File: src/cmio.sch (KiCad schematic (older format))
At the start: 3 parts

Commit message: Add LDO for 2.8V and 1.8V
Signed-off-by: Mahyar Koshkouei <deltabeard@users.noreply.github.com>
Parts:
- removed J?: TVOUT, symbol CONN_01X01_MALE
- added C1, C2, C5, C6: 1uF, symbol C_Small
- added C3, C4: 10nF, symbol C_Small
- added J2: USB_OTG, symbol USB_OTG
- added J4: CONN_COAXIAL, Connect:BNC, symbol CONN_COAXIAL
- added J5: CONN_02X20, Socket_Strips:Socket_Strip_Straight_2x20_Pitch2.54mm, symbol CONN_02X20
- added J6: Micro_SD_Card_TFP09_2_12B, symbol Micro_SD_Card_TFP09_2_12B
- added JP1: TP, Pin_Headers:Pin_Header_Straight_1x02_Pitch2.54mm, symbol Jumper_NC_Small
- added JP2: Disable SD Card, Pin_Headers:Pin_Header_Straight_1x02_Pitch2.54mm, symbol Jumper_NO_Small
- added SW1: SW_Push, Buttons_Switches_SMD:SW_SPST_TL3342, symbol SW_Push
- added U1: LD3985M18R, TO_SOT_Packages_SMD:SOT-23-5, symbol LD3985M18R
- added U2: LD3985M28R, TO_SOT_Packages_SMD:SOT-23-5, symbol LD3985M28R
- J1: renamed from J?; footprint (none) -> Socket_Strips:Socket_Strip_Straight_2x20_Pitch2.54mm
- gave numbers to parts that had none: 1
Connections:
- net labels added: CLK, CMD, DAT0, DAT1, DAT2, DAT3, DSI0, DSI0_0, DSI0_1, DSI0_2, DSI0_3, DSI0_4, DSI0_5, DSI1_0, DSI1_1, DSI1_2, DSI1_3, DSI1_4, DSI1_5, DSI1_6, DSI1_7, DSI1_8, DSI1_9, G28, G29, G30, G31, G32, G33, G34, G35, G36, G37, G38, G39, G40, G41, G42, G43, G44, G45, OTDIG, TVDAC
- net labels removed: +3.3V
- wire segments 3 -> 107
- no-connect marks 10 -> 46
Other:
- moved on the sheet: J1, J3

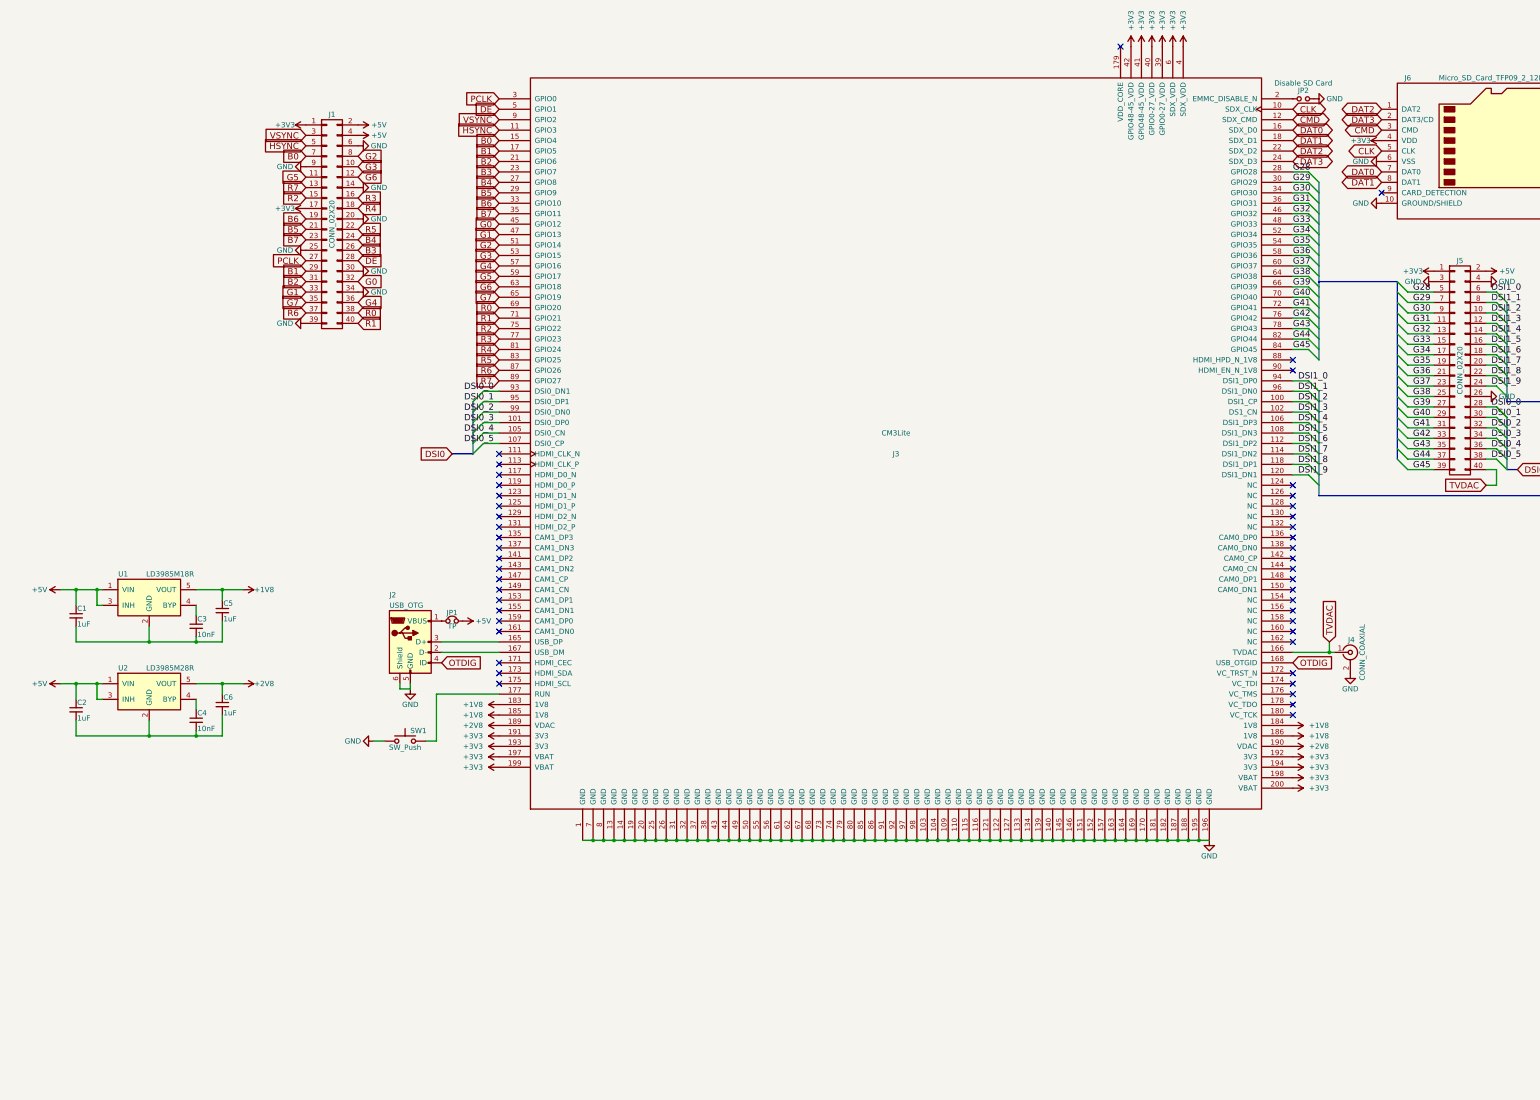
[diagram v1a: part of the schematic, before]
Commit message: Add Micro SD Card Footprint and 20-TQFP
Signed-off-by: Mahyar Koshkouei <deltabeard@users.noreply.github.com>
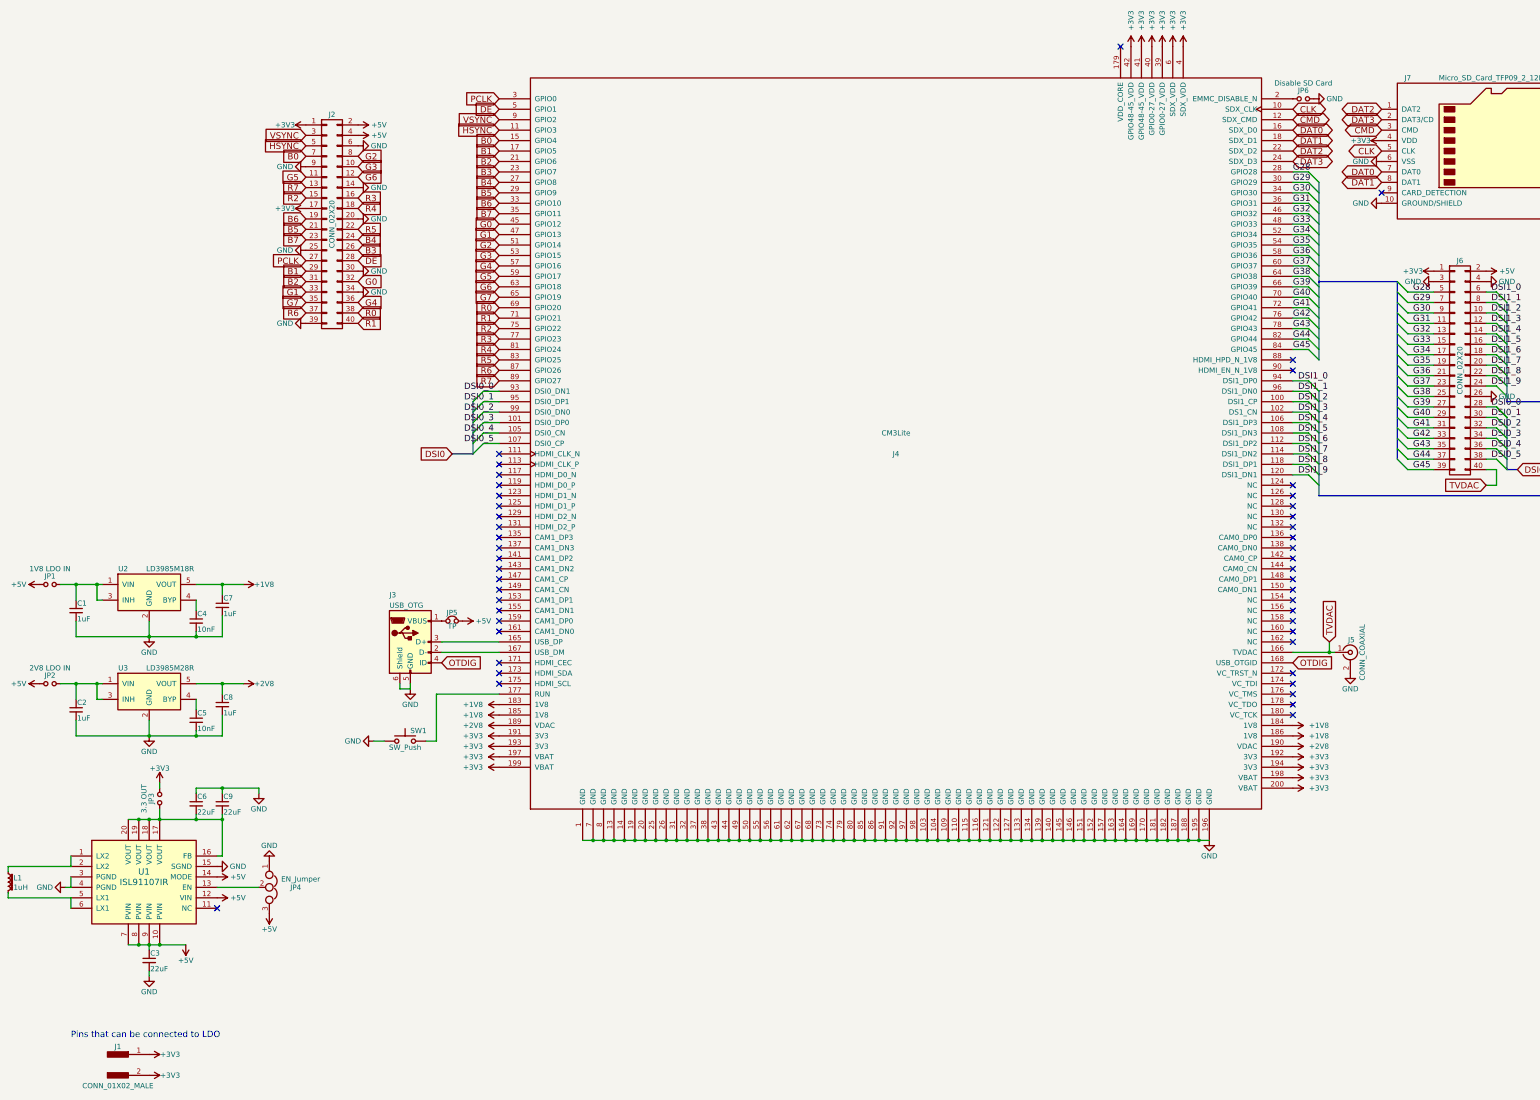
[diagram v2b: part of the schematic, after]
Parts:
- added C3, C6, C9: 22uF, Capacitors_SMD:C_1206_HandSoldering, symbol C_Small
- added J1: CONN_01X02_MALE, Pin_Headers:Pin_Header_Straight_1x02_Pitch2.54mm, symbol CONN_01X02_MALE
- added JP1: 1V8 LDO IN, Pin_Headers:Pin_Header_Straight_1x02_Pitch2.54mm, symbol Jumper_NO_Small
- added JP2: 2V8 LDO IN, Pin_Headers:Pin_Header_Straight_1x02_Pitch2.54mm, symbol Jumper_NO_Small
- added JP3: 3.3 OUT, Pin_Headers:Pin_Header_Straight_1x02_Pitch2.54mm, symbol Jumper_NO_Small
- added JP4: EN_Jumper, Socket_Strips:Socket_Strip_Straight_1x03_Pitch2.54mm, symbol Jumper_NC_Dual
- added L1: 1uH, Inductors:Inductor_Taiyo-Yuden_NR-40xx_HandSoldering, symbol L_Core_Ferrite_Small
- added U1: ISL91107IR, foot:20_TQFP, symbol ISL91107IR
- C1, C2: footprint (none) -> Capacitors_SMD:C_1206_HandSoldering
- C4: renamed from C3; footprint (none) -> Capacitors_SMD:C_1206_HandSoldering
- C5: renamed from C4; footprint (none) -> Capacitors_SMD:C_1206_HandSoldering
- C7: renamed from C5; footprint (none) -> Capacitors_SMD:C_1206_HandSoldering
- C8: renamed from C6; footprint (none) -> Capacitors_SMD:C_1206_HandSoldering
- renumbered J1 to J2, J2 to J3, J3 to J4, J4 to J5, J5 to J6, J6 to J7, JP1 to JP5, JP2 to JP6, U1 to U2, U2 to U3
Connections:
- net +3V3: now also J1.1, J1.2, JP3.2
- net +5V: now also C3.1, JP1.1, JP2.1, JP4.3, U1.10 (PVIN), U1.12 (VIN), U1.14 (MODE), U1.7 (PVIN), U1.8 (PVIN), U1.9 (PVIN); no longer C1.1, C2.1, U2.1 (VIN), U2.3 (INH), U3.1 (VIN), U3.3 (INH)
- net GND: now also C1.2, C2.2, C4.2, C5.2, C7.2, C8.2, U2.2 (GND), U3.2 (GND), C3.2, C6.1, C9.1, JP4.1, U1.15 (SGND), U1.3 (PGND), U1.4 (PGND)
- new net: C1.1, JP1.2, U2.1 (VIN), U2.3 (INH)
- new net: C2.1, JP2.2, U3.1 (VIN), U3.3 (INH)
- new net: L1.1, U1.1 (LX2), U1.2 (LX2)
- new net: JP4.2, U1.13 (EN)
- new net: C6.2, C9.2, JP3.1, U1.16 (FB), U1.17 (VOUT), U1.18 (VOUT), U1.19 (VOUT), U1.20 (VOUT)
- new net: L1.2, U1.5 (LX1), U1.6 (LX1)
- no-connect marks 46 -> 47
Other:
- note added: "Pins that can be connected to LDO"
- moved on the sheet: C1, C4, C7, U2

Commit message: Before removing RPi GPIO Compat
Signed-off-by: Mahyar Koshkouei <deltabeard@users.noreply.github.com>
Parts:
- added J8: CONN_01X06, Pin_Headers:Pin_Header_Straight_1x06_Pitch2.54mm, symbol CONN_01X06
- J3: footprint (none) -> foot:Micro_USB_B_10104110
- J5: footprint Connect:BNC -> foot:RCA_PHONO
- J7: footprint (none) -> foot:TFP09-2-12B
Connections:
- net +1V8: now also J6.34 (P34)
- net +2V8: now also J6.32 (P32)
- net +3V3: now also J6.30 (P30)
- net +5V: now also J6.28 (P28)
- net DSI0_0: now also J8.6 (P6); no longer J6.28 (P28)
- net DSI0_1: now also J8.5 (P5); no longer J6.30 (P30)
- net DSI0_2: now also J8.4 (P4); no longer J6.32 (P32)
- net DSI0_3: now also J8.3 (P3); no longer J6.34 (P34)
- net DSI0_4: now also J8.2 (P2); no longer J6.36 (P36)
- net DSI0_5: now also J8.1 (P1); no longer J6.38 (P38)
- net GND: now also J6.36 (P36), J6.38 (P38)
- net D+: now reaches J3.3 (D+), J4.165 (USB_DP)
- net D-: now reaches J3.2 (D-), J4.167 (USB_DM)
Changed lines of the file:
@@
 LIBS:Zilog
 LIBS:cmio-cache
-EELAYER 25 0
+EELAYER 26 0
 EELAYER END
 $Descr A3 16535 11693
@@
 F 0 "J3" H 4700 7200 50  0000 L CNN
 F 1 "USB_OTG" H 4700 7100 50  0000 L CNN
-F 2 "" H 5050 6700 50  0001 C CNN
+F 2 "foot:Micro_USB_B_10104110" H 5050 6700 50  0001 C CNN
 F 3 "" H 5050 6700 50  0001 C CNN
 	1    4900 6750
@@
 F 0 "J7" H 14450 2750 50  0000 C CNN
 F 1 "Micro_SD_Card_TFP09_2_12B" H 15750 2750 50  0000 R CNN
-F 2 "" H 17150 2750 50  0001 C CNN
+F 2 "foot:TFP09-2-12B" H 17150 2750 50  0001 C CNN
 F 3 "" H 15100 2150 50  0001 C CNN
 	1    15100 2050
@@
 F 0 "J5" H 13910 6970 50  0000 C CNN
 F 1 "CONN_COAXIAL" V 14015 6850 50  0000 C CNN
-F 2 "Connect:BNC" H 13900 6850 50  0001 C CNN
+F 2 "foot:RCA_PHONO" H 13900 6850 50  0001 C CNN
 F 3 "" H 13900 6850 50  0001 C CNN
 	1    13900 6850
@@
 Entry Wire Line
 	5500 4950 5600 4850
-Text GLabel 5300 4950 0    60   Input ~ 0
-DSI0
 Text Label 5700 4350 2    60   ~ 0
 DSI0_0
@@
 Text Label 5700 4850 2    60   ~ 0
 DSI0_5
-Text GLabel 15500 5100 2    60   Input ~ 0
-DSI0
-Entry Wire Line
-	15300 4500 15400 4600
-Entry Wire Line
-	15300 4500 15400 4600
-Entry Wire Line
-	15300 4600 15400 4700
-Entry Wire Line
-	15300 4700 15400 4800
-Entry Wire Line
-	15300 4800 15400 4900
-Entry Wire Line
-	15300 4900 15400 5000
-Entry Wire Line
-	15300 5000 15400 5100
-Text Label 15250 4500 0    60   ~ 0
+Entry Wire Line
+	4900 4350 5000 4450
+Entry Wire Line
+	4900 4350 5000 4450
+Entry Wire Line
+	4900 4450 5000 4550
+Entry Wire Line
+	4900 4550 5000 4650
+Entry Wire Line
+	4900 4650 5000 4750
+Entry Wire Line
+	4900 4750 5000 4850
+Entry Wire Line
+	4900 4850 5000 4950
+Text Label 4850 4350 0    60   ~ 0
 DSI0_0
-Text Label 15250 4600 0    60   ~ 0
+Text Label 4850 4450 0    60   ~ 0
 DSI0_1
-Text Label 15250 4700 0    60   ~ 0
+Text Label 4850 4550 0    60   ~ 0
 DSI0_2
-Text Label 15250 4800 0    60   ~ 0
+Text Label 4850 4650 0    60   ~ 0
 DSI0_3
-Text Label 15250 4900 0    60   ~ 0
+Text Label 4850 4750 0    60   ~ 0
 DSI0_4
-Text Label 15250 5000 0    60   ~ 0
+Text Label 4850 4850 0    60   ~ 0
 DSI0_5
 $Comp
@@
 	5600 4850 5750 4850
 Wire Bus Line
-	5500 4450 5500 4950
+	5500 4950 5500 4450
 Wire Bus Line
-	5500 4950 5300 4950
+	5000 4950 5500 4950
 Wire Bus Line
 	15400 3500 15400 4450
@@
 	16000 4450 16000 5350
 Wire Bus Line
-	15500 5100 15400 5100
-Wire Bus Line
-	15400 5100 15400 4600
-Wire Wire Line
-	15200 4500 15300 4500
-Wire Wire Line
-	15200 4600 15300 4600
-Wire Wire Line
-	15200 4700 15300 4700
-Wire Wire Line
-	15200 4800 15300 4800
-Wire Wire Line
-	15200 4900 15300 4900
-Wire Wire Line
-	15200 5000 15300 5000
+	5000 4950 5000 4450
+Wire Wire Line
+	4800 4350 4900 4350
+Wire Wire Line
+	4800 4450 4900 4450
+Wire Wire Line
+	4800 4550 4900 4550
+Wire Wire Line
+	4800 4650 4900 4650
+Wire Wire Line
+	4800 4750 4900 4750
+Wire Wire Line
+	4800 4850 4900 4850
 Wire Wire Line
 	15200 5100 15300 5100
@@
 	-1   0    0    1
 $EndComp
+Text Label 5250 6750 0    60   ~ 0
+D+
+Text Label 5250 6850 0    60   ~ 0
+D-
+$Comp
+L +5V #PWR065
+U 1 1 5929EA8C
+P 15200 4500
+F 0 "#PWR065" H 15200 4350 50  0001 C CNN
+F 1 "+5V" V 15200 4700 50  0000 C CNN
+F 2 "" H 15200 4500 50  0001 C CNN
+F 3 "" H 15200 4500 50  0001 C CNN
+	1    15200 4500
+	0    1    1    0
+$EndComp
+$Comp
+L +3V3 #PWR066
+U 1 1 5929EB39
+P 15200 4600
+F 0 "#PWR066" H 15200 4450 50  0001 C CNN
+F 1 "+3V3" V 15200 4800 50  0000 C CNN
+F 2 "" H 15200 4600 50  0001 C CNN
+F 3 "" H 15200 4600 50  0001 C CNN
+	1    15200 4600
+	0    1    1    0
+$EndComp
+$Comp
+L GND #PWR067
+U 1 1 5929EBB0
+P 15200 5000
+F 0 "#PWR067" H 15200 4750 50  0001 C CNN
+F 1 "GND" V 15200 4800 50  0000 C CNN
+F 2 "" H 15200 5000 50  0001 C CNN
+F 3 "" H 15200 5000 50  0001 C CNN
+	1    15200 5000
+	0    -1   -1   0
+$EndComp
+$Comp
+L +2V8 #PWR068
+U 1 1 5929EDD1
+P 15200 4700
+F 0 "#PWR068" H 15200 4550 50  0001 C CNN
+F 1 "+2V8" V 15200 4900 50  0000 C CNN
+F 2 "" H 15200 4700 50  0001 C CNN
+F 3 "" H 15200 4700 50  0001 C CNN
+	1    15200 4700
+	0    1    1    0
+$EndComp
+$Comp
+L +1V8 #PWR069
+U 1 1 5929F02F
+P 15200 4800
+F 0 "#PWR069" H 15200 4650 50  0001 C CNN
+F 1 "+1V8" V 15200 5000 50  0000 C CNN
+F 2 "" H 15200 4800 50  0001 C CNN
+F 3 "" H 15200 4800 50  0001 C CNN
+	1    15200 4800
+	0    1    1    0
+$EndComp
+$Comp
+L GND #PWR070
+U 1 1 5929F285
+P 15200 4900
+F 0 "#PWR070" H 15200 4650 50  0001 C CNN
+F 1 "GND" V 15200 4700 50  0000 C CNN
+F 2 "" H 15200 4900 50  0001 C CNN
+F 3 "" H 15200 4900 50  0001 C CNN
+	1    15200 4900
+	0    -1   -1   0
+$EndComp
+$Comp
+L CONN_01X06 J8
+U 1 1 592A02D7
+P 4600 4600
+F 0 "J8" H 4519 4125 50  0000 C CNN
+F 1 "CONN_01X06" H 4519 4216 50  0000 C CNN
+F 2 "Pin_Headers:Pin_Header_Straight_1x06_Pitch2.54mm" H 4600 4600 50  0001 C CNN
+F 3 "" H 4600 4600 50  0001 C CNN
+	1    4600 4600
+	-1   0    0    1
+$EndComp
